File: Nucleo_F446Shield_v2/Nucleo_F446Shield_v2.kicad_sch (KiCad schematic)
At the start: 48 parts, among them J1 Barrel_Jack, J11 CAN1, J12 CAN2, J15 CAN1, J16 CAN2, J19 I2C3, J20 UART4, J21 xt60 male, J3 CAN1, J4 CAN2, J7 CAN1, J8 CAN2, M3 TJA1050_Module, M4 TJA1050_Module, SW1 SW1, SW11 DIP1, SW2 SW2, SW3 SW3, U1 NUCLEO-F446RE, U2 MP1584

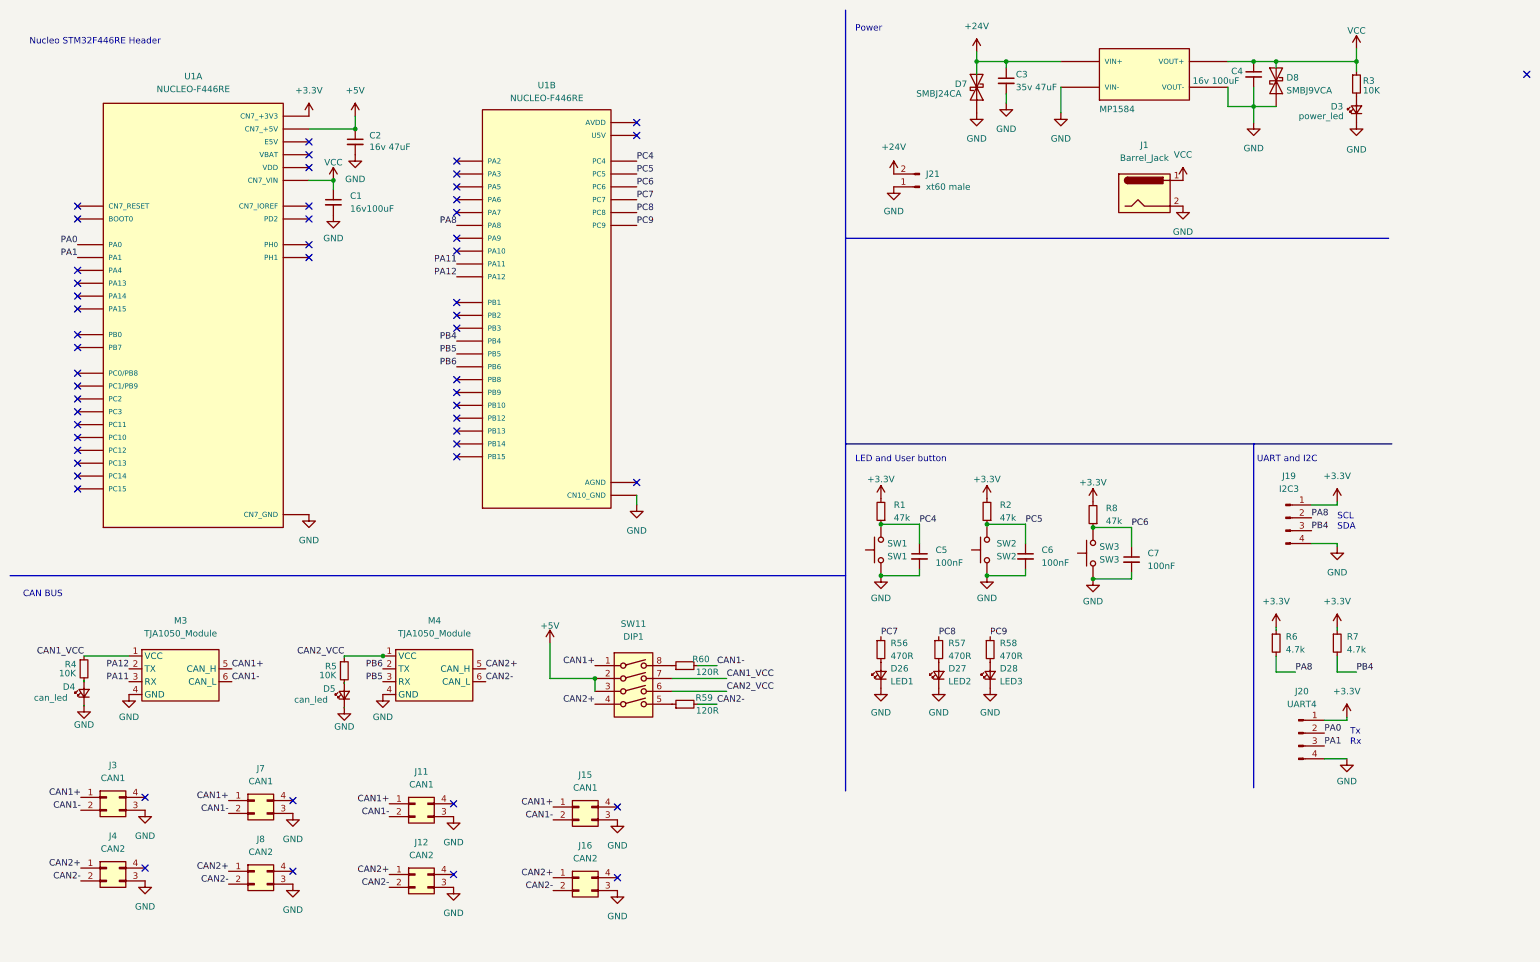
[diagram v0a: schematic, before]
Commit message: add V2 board
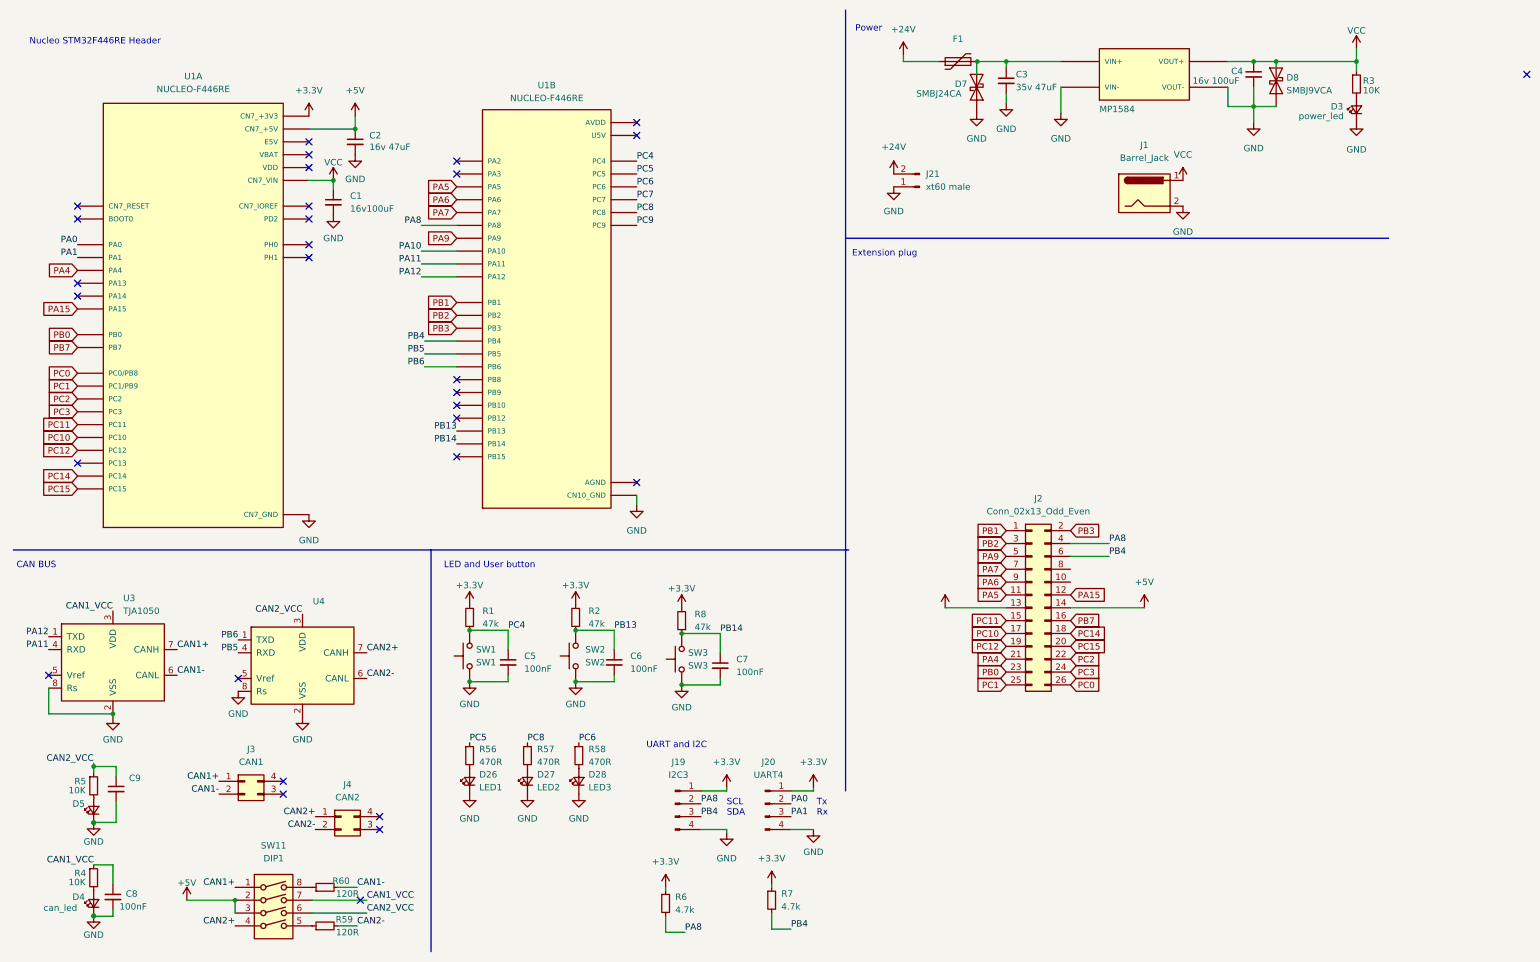
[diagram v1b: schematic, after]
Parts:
- removed J11, J15, J7: CAN1, Connector_Molex:Molex_Micro-Fit_3.0_43045-0412_2x02_P3.00mm_Vertical, symbol Connector_Generic:Conn_02x02_Counter_Clockwise
- removed J12, J16, J8: CAN2, Connector_Molex:Molex_Micro-Fit_3.0_43045-0412_2x02_P3.00mm_Vertical, symbol Connector_Generic:Conn_02x02_Counter_Clockwise
- removed M3, M4: TJA1050_Module, PolyuRobotics:TJA1050_CAN_Module, symbol PolyuRobotics:TJA1050_Module
- added C8: 100nF, symbol Device:C_Small
- added C9: (no value), symbol Device:C_Small
- added F1: (no value), symbol Device:Polyfuse
- added J2: Conn_02x13_Odd_Even, symbol Connector_Generic:Conn_02x13_Odd_Even
- added U3: TJA1050, Package_SO:SOIC-8_3.9x4.9mm_P1.27mm, symbol Interface_CAN_LIN:MCP2551-I-SN
- added U4: (no value), Package_SO:SOIC-8_3.9x4.9mm_P1.27mm, symbol Interface_CAN_LIN:MCP2551-I-SN
- D5: value can_led -> (none)
- J3, J4: footprint Connector_Molex:Molex_Micro-Fit_3.0_43045-0412_2x02_P3.00mm_Vertical -> (none)
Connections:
- net +24V: now also F1.1; no longer C3.1, D7.1 (K), U2.IN1+ (VIN+), U2.IN2+ (VIN+)
- net +5V: now also J2.13 (Pin_13), J2.14 (Pin_14)
- net CAN1+: now also U3.7 (CANH)
- net CAN1-: now also U3.6 (CANL)
- net CAN1_VCC: now also C8.1, U3.3 (VDD)
- net CAN2+: now also U4.7 (CANH)
- net CAN2-: now also U4.6 (CANL)
- net CAN2_VCC: now also C9.1, U4.3 (VDD)
- net GND: now also C8.2, C9.2, U3.2 (VSS), U3.8 (Rs), U4.2 (VSS), U4.8 (Rs); no longer J3.3 (Pin_3), J4.3 (Pin_3)
- net PA11: now also U3.4 (RXD)
- net PA12: now also U3.1 (TXD)
- net PA8: now also J2.4 (Pin_4)
- net PB4: now also J2.6 (Pin_6)
- net PB5: now also U4.4 (RXD)
- net PB6: now also U4.1 (TXD)
- net PC5: now also R56.1; no longer C6.1, R2.1, SW2.2
- net PC6: now also R58.1; no longer C7.1, R8.1, SW3.2
- net PC7: no longer R56.1
- net PC9: no longer R58.1
- net PC10: now reaches U1.CN7_1 (PC10)
- net PC10: now also J2.17 (Pin_17)
- net PA15: now reaches U1.CN7_17 (PA15)
- net PA15: now also J2.12 (Pin_12)
- net PC11: now reaches U1.CN7_2 (PC11)
- net PC11: now also J2.15 (Pin_15)
- net PB7: now reaches U1.CN7_21 (PB7)
- net PB7: now also J2.16 (Pin_16)
- net PC14: now reaches U1.CN7_25 (PC14)
- net PC14: now also J2.18 (Pin_18)
- net PC15: now reaches U1.CN7_27 (PC15)
- net PC15: now also J2.20 (Pin_20)
- net PC12: now reaches U1.CN7_3 (PC12)
- net PC12: now also J2.19 (Pin_19)
- net PA4: now reaches U1.CN7_32 (PA4)
- net PA4: now also J2.21 (Pin_21)
- net PB0: now reaches U1.CN7_34 (PB0)
- net PB0: now also J2.23 (Pin_23)
- net PC2: now reaches U1.CN7_35 (PC2)
- net PC2: now also J2.22 (Pin_22)
- net PC1: now reaches U1.CN7_36 (PC1/PB9)
- net PC1: now also J2.25 (Pin_25)
- net PC3: now reaches U1.CN7_37 (PC3)
- net PC3: now also J2.24 (Pin_24)
- net PC0: now reaches U1.CN7_38 (PC0/PB8)
- net PC0: now also J2.26 (Pin_26)
- net PA5: now reaches U1.CN10_11 (PA5)
- net PA5: now also J2.11 (Pin_11)
- net PA6: now reaches U1.CN10_13 (PA6)
- net PA6: now also J2.9 (Pin_9)
- net PA7: now reaches U1.CN10_15 (PA7)
- net PA7: now also J2.7 (Pin_7)
- net PA9: now reaches U1.CN10_21 (PA9)
- net PA9: now also J2.5 (Pin_5)
- net PB2: now reaches U1.CN10_22 (PB2)
- net PB2: now also J2.3 (Pin_3)
- net PB1: now reaches U1.CN10_24 (PB1)
- net PB1: now also J2.1 (Pin_1)
- net PB14: now reaches U1.CN10_28 (PB14)
- net PB14: now also C7.1, R8.1, SW3.2
- net PB13: now reaches U1.CN10_30 (PB13)
- net PB13: now also C6.1, R2.1, SW2.2
- net PB3: now reaches U1.CN10_31 (PB3)
- net PB3: now also J2.2 (Pin_2)
- net PA10: now reaches U1.CN10_33 (PA10)
- new net: C3.1, D7.1 (K), F1.2, U2.IN1+ (VIN+), U2.IN2+ (VIN+)
- no-connect marks 54 -> 30
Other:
- note added: "Extension plug"
- moved on the sheet: C5, C6, C7, D26, D27, D28, D4, D5, J19, J20, J3, J4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

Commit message: add V2 board
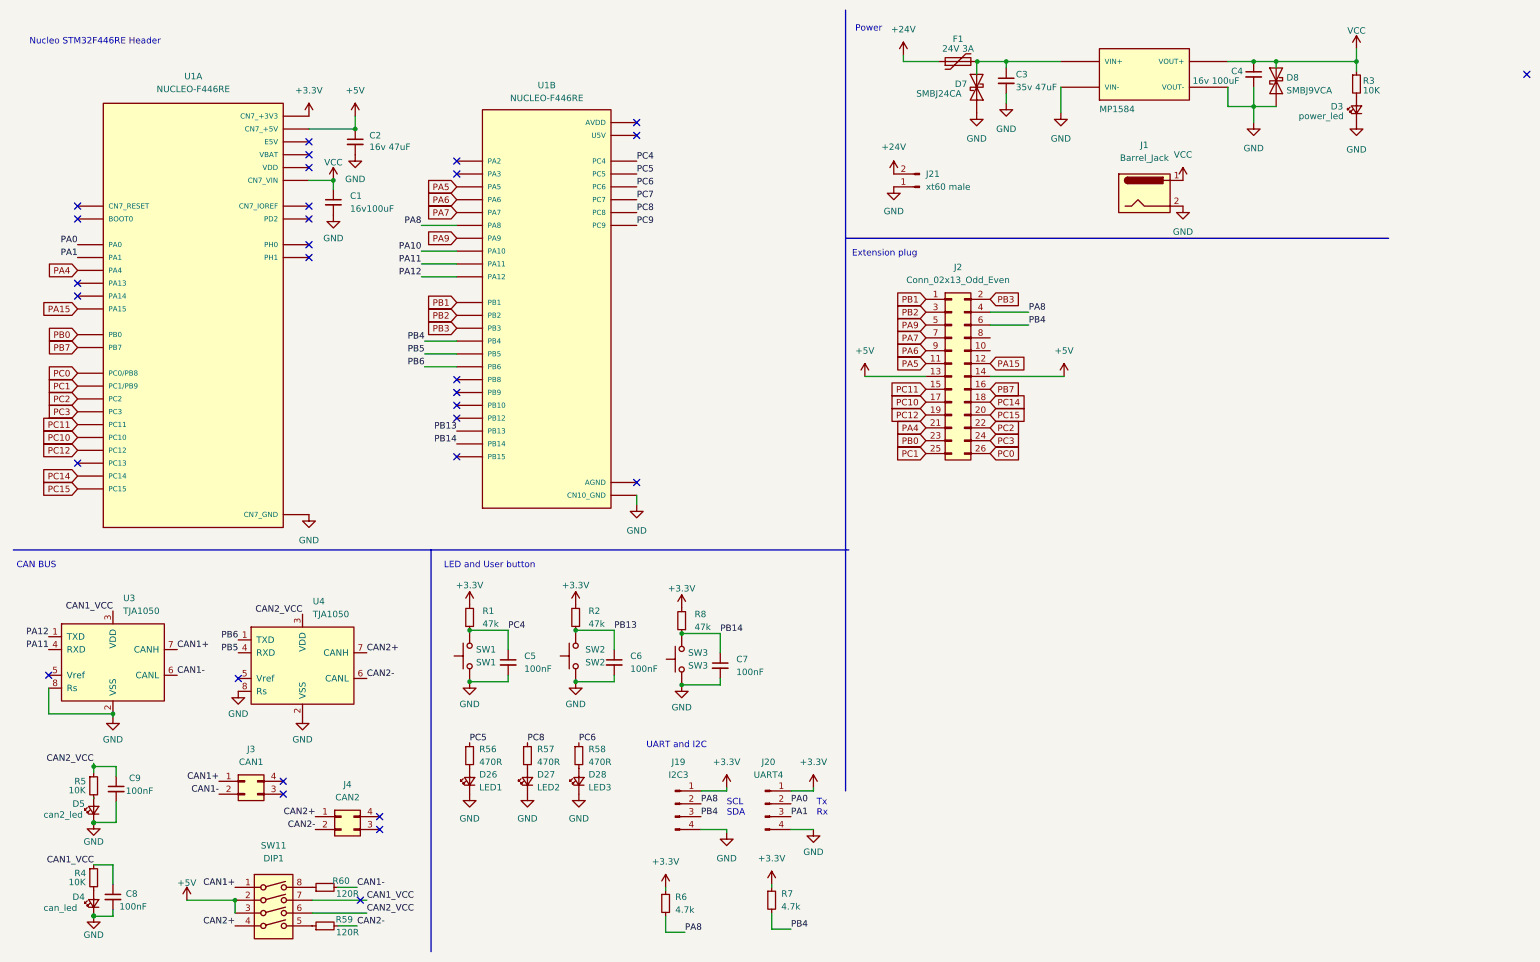
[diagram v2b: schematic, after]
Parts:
- C8: footprint (none) -> Capacitor_SMD:C_0805_2012Metric_Pad1.18x1.45mm_HandSolder
- C9: value (none) -> 100nF; footprint (none) -> Capacitor_SMD:C_0805_2012Metric_Pad1.18x1.45mm_HandSolder
- D5: value (none) -> can2_led
- F1: value (none) -> 24V 3A; footprint (none) -> Fuse:Fuse_1812_4532Metric_Pad1.30x3.40mm_HandSolder
- J2: footprint (none) -> Connector_IDC:IDC-Header_2x13_P2.54mm_Vertical
- J3, J4: footprint (none) -> Connector_Molex:Molex_Micro-Fit_3.0_43045-0400_2x02_P3.00mm_Horizontal
- U4: value (none) -> TJA1050
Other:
- moved on the sheet: J2

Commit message: added NucleoF446
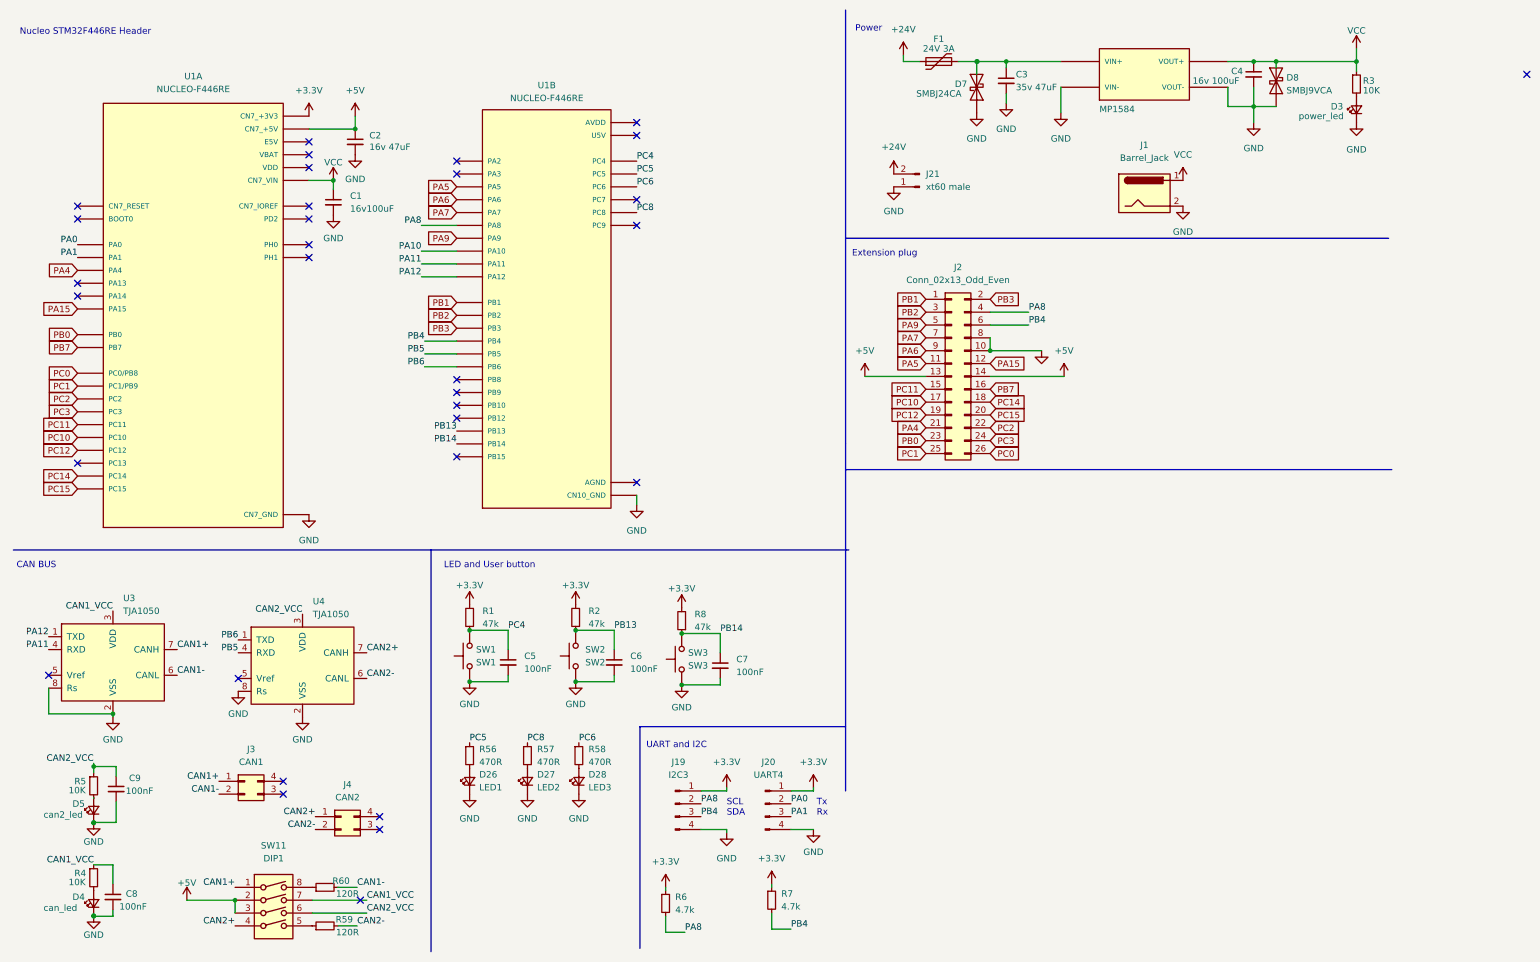
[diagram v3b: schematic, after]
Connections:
- net GND: now also J2.10 (Pin_10), J2.8 (Pin_8)
- net PC7: no longer names the net of U1.CN10_19 (PC7)
- net PC9: no longer names the net of U1.CN10_1 (PC9)
- no-connect marks 30 -> 32
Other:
- company: (none) -> PolyU Robotics Club
- title: (none) -> Nucleo-F446 Shield
- moved on the sheet: F1
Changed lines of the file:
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@@
 (kicad_sch (version 20211123) (generator eeschema)
   (paper "A4")
+  (title_block
+    (title "Nucleo-F446 Shield")
+    (date "2022-04-07")
+    (rev "v1.5")
+    (company "PolyU Robotics Club")
+  )
   (junction (at 28.575 172.72) (diameter 0) (color 0 0 0 0)
   )
@@
   (junction (at 80.264 35.56) (diameter 0) (color 0 0 0 0)
   )
+  (junction (at 203.073 22.225) (diameter 0) (color 0 0 0 0)
+  )
   (junction (at 28.575 191.008) (diameter 0) (color 0 0 0 0)
   )
@@
   )
   (junction (at 28.575 191.135) (diameter 0) (color 0 0 0 0)
+  )
+  (junction (at 205.74 79.375) (diameter 0) (color 0 0 0 0)
   )
   (junction (at 56.515 187.96) (diameter 0) (color 0 0 0 0)
@@
   (no_connect (at 25.4 101.6))
   (no_connect (at 135.89 105.41))
+  (no_connect (at 135.89 54.61))
   (no_connect (at 311.785 24.765))
   (no_connect (at 71.12 58.42))
@@
   (no_connect (at 25.4 66.04))
   (no_connect (at 71.12 43.18))
+  (no_connect (at 135.89 49.53))
   (no_connect (at 100.33 100.33))
   (no_connect (at 100.33 85.09))
@@
     (stroke (width 0) (type default) (color 0 0 0 0))
   )
+  (polyline (pts (xy 136.525 153.67) (xy 136.525 197.485))
+    (stroke (width 0) (type default) (color 0 0 0 0))
+  )
   (wire (pts (xy 82.55 190.5) (xy 71.755 190.5))
     (stroke (width 0) (type default) (color 0 0 0 0))
@@
     (stroke (width 0) (type default) (color 0 0 0 0))
   )
+  (wire (pts (xy 199.39 22.225) (xy 203.073 22.225))
+    (stroke (width 0) (type default) (color 0 0 0 0))
+  )
   (polyline (pts (xy 177.165 12.065) (xy 177.165 97.79))
     (stroke (width 0) (type default) (color 0 0 0 0))
@@
     (stroke (width 0) (type default) (color 0 0 0 0))
   )
+  (wire (pts (xy 205.74 76.835) (xy 205.74 79.375))
+    (stroke (width 0) (type default) (color 0 0 0 0))
+  )
   (wire (pts (xy 123.825 134.62) (xy 131.445 134.62))
     (stroke (width 0) (type default) (color 0 0 0 0))
@@
     (stroke (width 0) (type default) (color 0 0 0 0))
   )
+  (wire (pts (xy 215.9 79.375) (xy 205.74 79.375))
+    (stroke (width 0) (type default) (color 0 0 0 0))
+  )
   (wire (pts (xy 93.345 54.61) (xy 100.33 54.61))
     (stroke (width 0) (type default) (color 0 0 0 0))
@@
     (stroke (width 0) (type default) (color 0 0 0 0))
   )
+  (polyline (pts (xy 177.165 102.87) (xy 285.115 102.87))
+    (stroke (width 0) (type default) (color 0 0 0 0))
+  )
   (polyline (pts (xy 177.165 97.79) (xy 177.165 166.37))
     (stroke (width 0) (type default) (color 0 0 0 0))
@@
     (stroke (width 0) (type default) (color 0 0 0 0))
   )
+  (polyline (pts (xy 177.165 153.67) (xy 136.525 153.67))
+    (stroke (width 0) (type default) (color 0 0 0 0))
+  )
   (wire (pts (xy 252.73 22.225) (xy 257.81 22.225))
     (stroke (width 0) (type default) (color 0 0 0 0))
@@
     (stroke (width 0) (type default) (color 0 0 0 0))
   )
-  (wire (pts (xy 188.595 22.225) (xy 195.58 22.225))
+  (wire (pts (xy 188.595 22.225) (xy 191.77 22.225))
     (stroke (width 0) (type default) (color 0 0 0 0))
   )
@@
     (effects (font (size 1.27 1.27)) (justify left bottom))
   )
-  (text "Nucleo STM32F446RE Header" (at 15.875 19.05 0)
+  (text "Nucleo STM32F446RE Header" (at 13.97 17.145 0)
     (effects (font (size 1.27 1.27)) (justify left bottom))
   )
@@
     (effects (font (size 1.27 1.27)) (justify right bottom))
   )
-  (label "PC9" (at 135.89 54.61 0)
-    (effects (font (size 1.27 1.27)) (justify left bottom))
-  )
   (label "PB14" (at 152.4 135.255 0)
     (effects (font (size 1.27 1.27)) (justify left bottom))
@@
   )
   (label "CAN2_VCC" (at 82.55 190.5 0)
-    (effects (font (size 1.27 1.27)) (justify left bottom))
-  )
-  (label "PC7" (at 135.89 49.53 0)
     (effects (font (size 1.27 1.27)) (justify left bottom))
   )
@@
     (pin "2")
   )
+  (symbol (lib_id "power:GND") (at 215.9 79.375 0) (unit 1)
+    (in_bom yes) (on_board yes) (fields_autoplaced)
+    (property "Reference" "#PWR0123" (id 0) (at 215.9 85.725 0)
+      (effects (font (size 1.27 1.27)) hide)
+    )
+    (property "Value" "" (id 1) (at 215.9 83.82 0))
+    (property "Footprint" "" (id 2) (at 215.9 79.375 0)
+      (effects (font (size 1.27 1.27)) hide)
+    )
+    (property "Datasheet" "" (id 3) (at 215.9 79.375 0)
+      (effects (font (size 1.27 1.27)) hide)
+    )
+    (pin "1")
+  )
   (symbol (lib_id "Device:LED_Small") (at 114.3 164.465 90) (unit 1)
     (in_bom yes) (on_board yes) (fields_autoplaced)
@@
     (pin "1")
   )
-  (symbol (lib_id "Device:Polyfuse") (at 199.39 22.225 90) (unit 1)
-    (in_bom yes) (on_board yes)
-    (property "Reference" "F1" (id 0) (at 199.39 17.78 90))
-    (property "Value" "24V 3A" (id 1) (at 199.39 19.685 90))
-    (property "Footprint" "Fuse:Fuse_1812_4532Metric_Pad1.30x3.40mm_HandSolder" (id 2) (at 204.47 20.955 0)
+  (symbol (lib_id "Device:Polyfuse") (at 195.58 22.225 90) (unit 1)
+    (in_bom yes) (on_board yes)
+    (property "Reference" "F1" (id 0) (at 195.58 17.78 90))
+    (property "Value" "24V 3A" (id 1) (at 195.58 19.685 90))
+    (property "Footprint" "Fuse:Fuse_1812_4532Metric_Pad1.30x3.40mm_HandSolder" (id 2) (at 200.66 20.955 0)
       (effects (font (size 1.27 1.27)) (justify left) hide)
     )
-    (property "Datasheet" "~" (id 3) (at 199.39 22.225 0)
+    (property "Datasheet" "~" (id 3) (at 195.58 22.225 0)
       (effects (font (size 1.27 1.27)) hide)
     )
@@
       (reference "#PWR0122") (unit 1) (value "+5V") (footprint "")
     )
+    (path "/203090e4-55b5-4296-8f59-81cdb9f4e79b"
+      (reference "#PWR0123") (unit 1) (value "GND") (footprint "")
+    )
     (path "/3abd7469-55d0-47a2-af64-a451c3080b07"
